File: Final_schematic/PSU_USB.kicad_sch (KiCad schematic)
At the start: 25 parts, among them J4 USB_C_Receptacle_USB2.0_16P, U2 LM27762, U3 HT75xx-1-SOT89

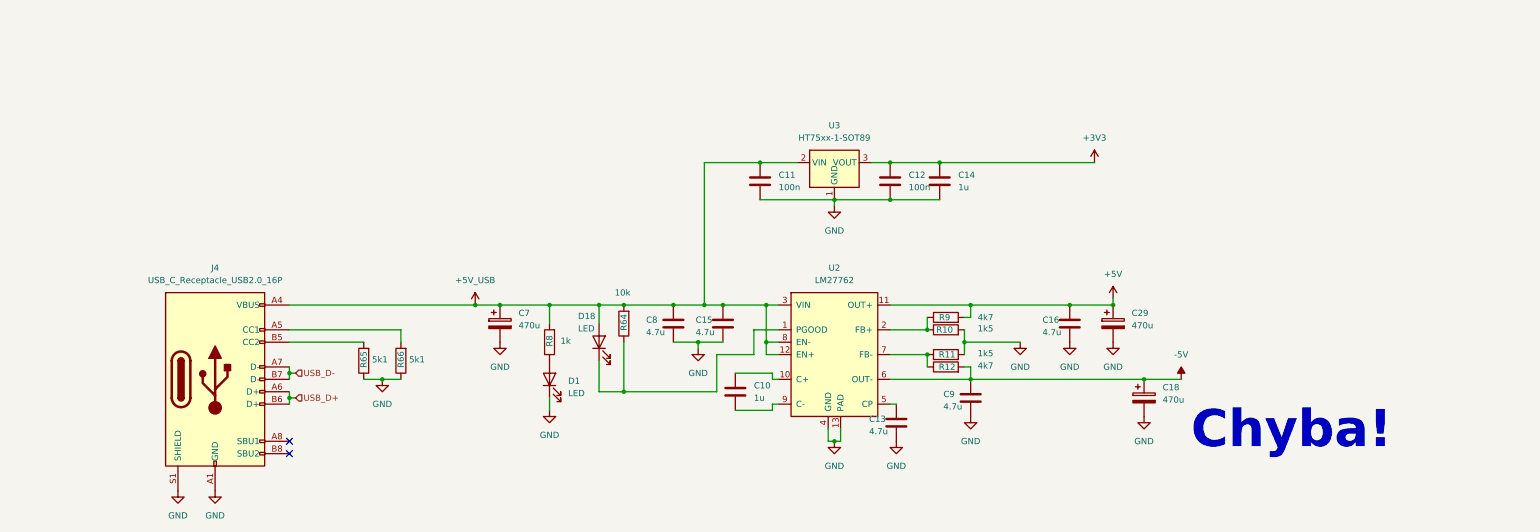
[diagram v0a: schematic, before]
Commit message: Removed obsolete PDF files and updated LaTeX documents with new sections and references.
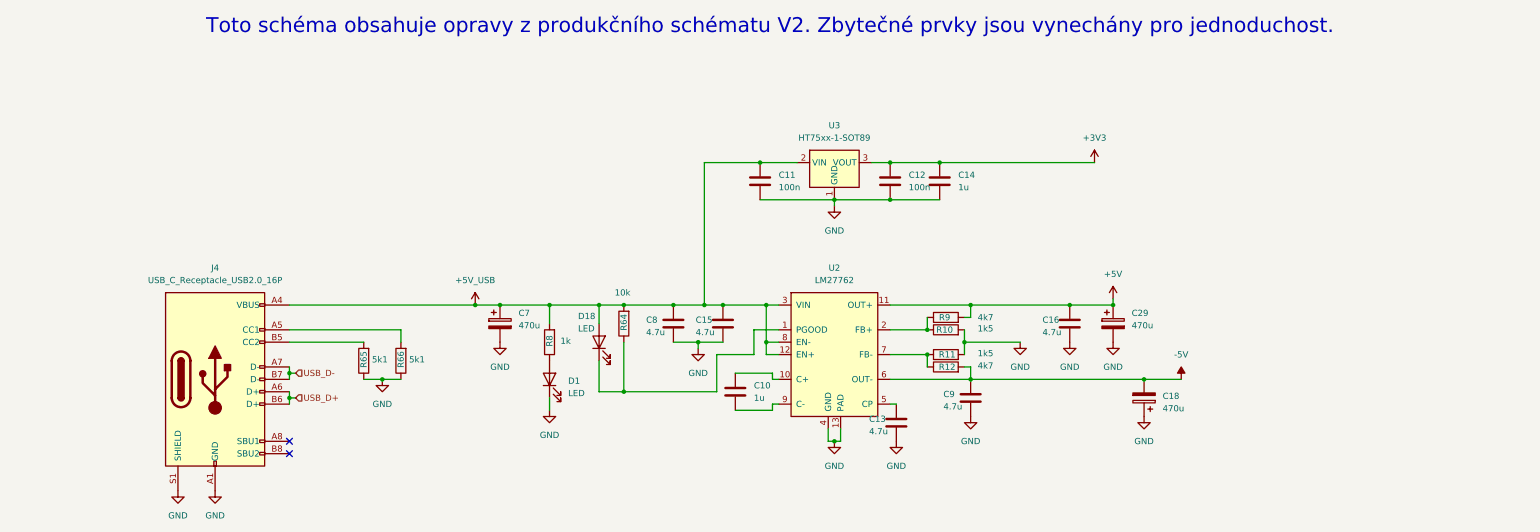
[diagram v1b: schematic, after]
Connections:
- net -5V: now also C18.2; no longer C18.1
- net GND: now also C18.1; no longer C18.2
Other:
- note added: "Toto schéma obsahuje opravy z produkčního schématu V2. Zbytečné prvky jsou vynechány pro jednoduchost."
- note removed: "Chyba!"
- moved on the sheet: C18
